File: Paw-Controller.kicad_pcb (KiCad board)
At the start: 2 copper layers, 41 x 24 mm, 26 parts, among them J1 Conn_02x06_Odd_Even, J2 Conn_01x08, J3 Conn_01x02, Q1 DMN1019USN, Q2 DMN1019USN, Q3 DMN1019USN, SW1 SW_SPST_KMR2, U1 LMZ10503, U2 ATSAMD21E18A-AF

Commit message: Added missing PWM labels.
Signed-off-by: Aaron Williams <aaron.w2@gmail.com>
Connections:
- net Net-(D1-Pad2) renamed /PWM0
- net Net-(D2-Pad2) renamed /PWM1
- net Net-(D3-Pad2) renamed /PWM2

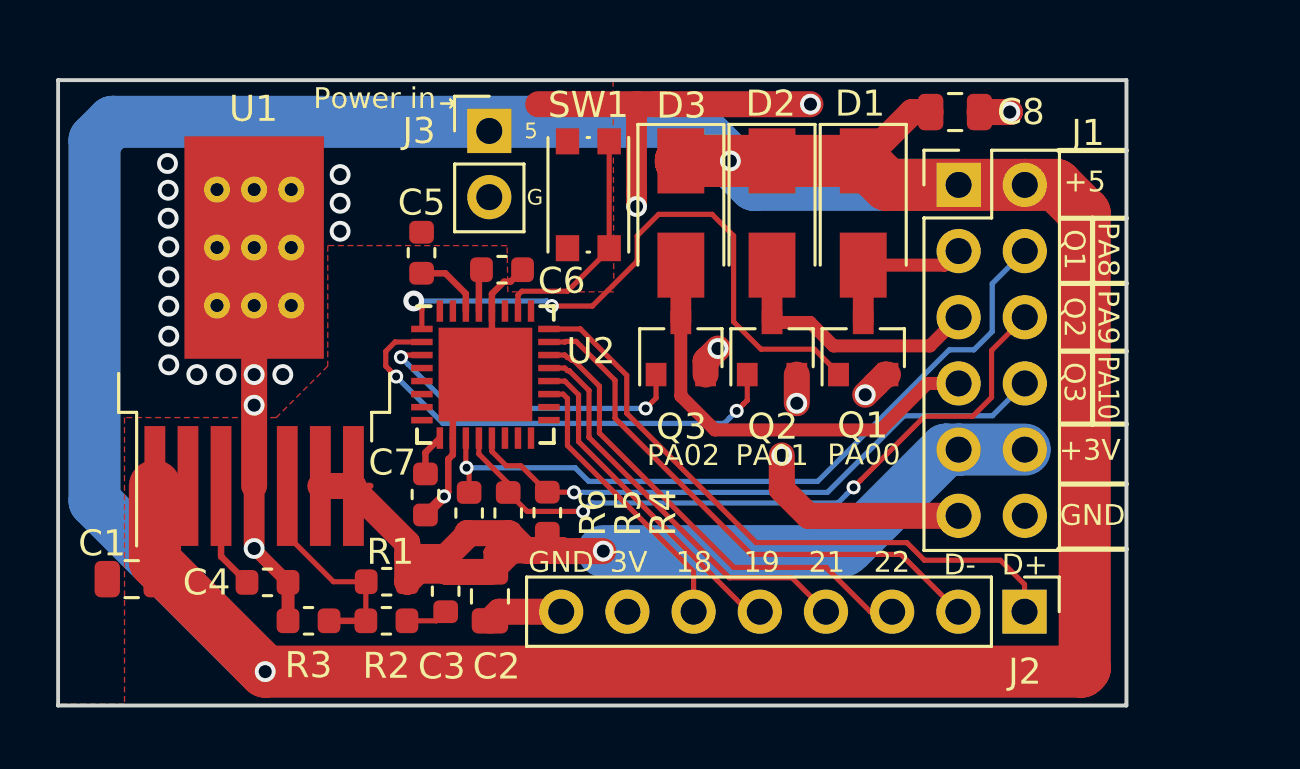
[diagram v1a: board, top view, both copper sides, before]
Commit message: Version 2.0 converts each PWM channel to use an H-bridge.
This allows the controller to be able to drive a 3V brushless motor.  The
M0 processor is capable of generating the timing for the motors, though at
this time I don't know if it works with 6 GPIO pins or only with three.

Six was chosen so that a PWMs can be set to a high impedence state.  This
is useful in the case where multiple brushed motors are attached between either
+3v or ground and the PWM pin, though the alternative is to just pull the PWM
output to the same level.  That might be version 2.1 later.

Signed-off-by: Aaron Williams <aaron.w2@gmail.com>
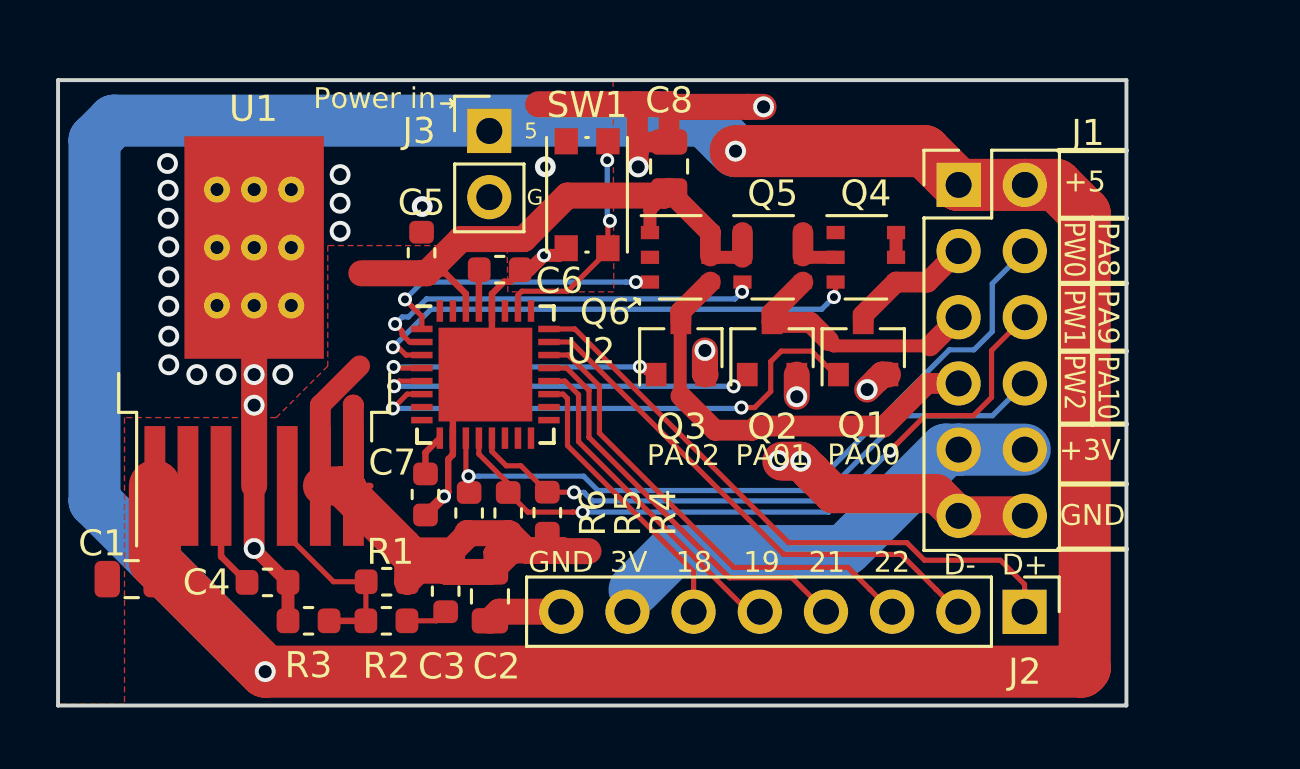
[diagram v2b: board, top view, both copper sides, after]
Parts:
- removed D1, D2, D3: B120-E3, Diode_SMD:D_SMA
- added Q4: SI3493DDV-T1-GE3, Package_SO:TSOP-6_1.65x3.05mm_P0.95mm, F.Cu at (80.0, 69.8)
- added Q5: SI3493DDV-T1-GE3, Package_SO:TSOP-6_1.65x3.05mm_P0.95mm, F.Cu at (76.4, 69.8)
- added Q6: SI3493DDV-T1-GE3, Package_SO:TSOP-6_1.65x3.05mm_P0.95mm, F.Cu at (72.9, 69.8)
- moved C8 11.2 mm to (72.5, 66.3), turned to 90 degrees
- moved C6 0.09 mm to (66.0, 70.3)
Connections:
- C8 pad 1: +5V -> +3V3
- Q1 pad 1: /PA00 -> /PA05
- Q2 pad 1: /PA01 -> /PA04
- Q3 pad 1: /PA02 -> /PA03
- U2 pad 4: Net-(U2-Pad4) -> /PA03
- U2 pad 5: Net-(U2-Pad5) -> /PA04
- U2 pad 6: Net-(U2-Pad6) -> /PA05
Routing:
- net +3V3: track 47.9 -> 85.4 mm, vias 1 -> 0
- net /PA05: track 0.00 -> 20.4 mm, vias 0 -> 2
- net +5V: track 138.3 -> 122.0 mm
- net /PA04: track 0.00 -> 14.9 mm, vias 0 -> 2
- net /PA00: track 24.1 -> 11.1 mm
- net /PA03: track 0.00 -> 11.3 mm, vias 0 -> 2
- net /PA02: track 12.5 -> 19.6 mm
- net /PA01: track 18.2 -> 15.6 mm
- net GND: track 58.1 -> 59.4 mm, vias 25 -> 28
- net /D_N: track 20.9 -> 20.0 mm
- net /D_P: track 24.2 -> 23.4 mm
- net /PWM2: track 17.0 -> 17.7 mm
- net Net-(SW1-Pad2): track 8.99 -> 9.07 mm, vias 0 -> 2
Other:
- board text added: "Do not exceed 5V for PWM0, PWM1 or PWM2."
- board text added: "PW0"
- board text added: "PW1"
- board text added: "PW2"
- board text added: "Rev 2.0"
- board text removed: "Do not exceed 5V for Q0, Q1 and Q2 due to protection diodes."
- board text removed: "Q1"
- board text removed: "Q2"
- board text removed: "Q3"
- board text removed: "Rev 1.0"

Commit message: Fixed solder mask clearance.
Signed-off-by: Aaron Williams <aaron.w2@gmail.com>
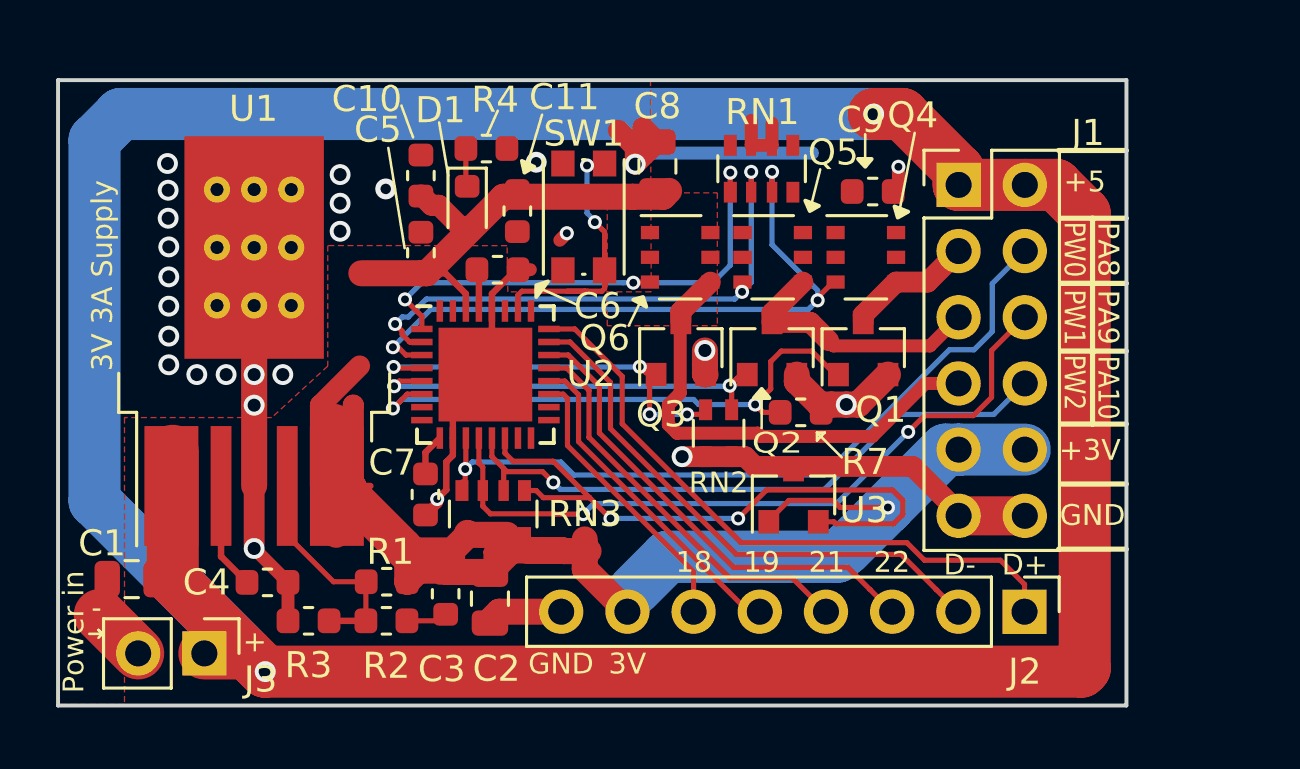
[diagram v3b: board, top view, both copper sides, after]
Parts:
- removed R5, R6: 10K, Resistor_SMD:R_0603_1608Metric
- added C10: 1uF, Capacitor_SMD:C_0603_1608Metric, F.Cu at (62.9, 66.7)
- added C11: 0.1uF, Capacitor_SMD:C_0603_1608Metric, F.Cu at (66.6, 68.0)
- added C9: 0.1uF, Capacitor_SMD:C_0603_1608Metric, F.Cu at (80.3, 67.3)
- added D1: LED, LED_SMD:LED_0603_1608Metric, F.Cu at (64.7, 67.9)
- added R7: 100K, Resistor_SMD:R_0603_1608Metric, F.Cu at (77.5, 75.8)
- added RN1: 100K, Resistor_SMD:R_Array_Convex_4x0603, F.Cu at (76.0, 66.4)
- added RN2: 100K, Resistor_SMD:R_Array_Convex_2x0603, F.Cu at (74.3, 76.5)
- added RN3: 10K, Resistor_SMD:R_Array_Convex_4x0603, F.Cu at (65.7, 79.7)
- added U3: DRV5032FCDBZT, Package_TO_SOT_SMD:SOT-23, F.Cu at (77.2, 79.0)
- R4: value 10K -> 330
- moved J3 22.8 mm to (54.6, 85.0), turned to 270 degrees
- moved R4 14.2 mm to (65.4, 65.6), turned to 180 degrees
- moved SW1 0.86 mm to (69.2, 68.2)
- moved C8 0.45 mm to (72.0, 66.3)
- moved C3 0.10 mm to (63.9, 82.7)
- moved C2 0.09 mm to (65.6, 82.9)
- moved C6 0.09 mm to (65.9, 70.3)
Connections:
- R4 pad 1: +3V3 -> GND
- R4 pad 2: /PA10 -> Net-(D1-Pad1)
- U2 pad 14: Net-(U2-Pad14) -> /PA11
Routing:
- net /PA11: track 0.00 -> 24.1 mm, vias 0 -> 2
- net /PA00: track 11.1 -> 19.4 mm, vias 2 -> 3
- net GND: track 59.4 -> 66.1 mm, vias 28 -> 26
- net /PA02: track 19.6 -> 25.8 mm, vias 2 -> 3
- net /PA01: track 15.6 -> 21.1 mm, vias 2 -> 3
- net +3V3: track 85.4 -> 90.6 mm, vias 0 -> 1
- net +5V: track 122.0 -> 126.2 mm
- net /PA03: track 11.3 -> 15.2 mm, vias 2 -> 4
- net Net-(D1-Pad1): track 0.00 -> 1.52 mm
- net Net-(SW1-Pad2): track 9.07 -> 10.4 mm
- net /PA05: track 20.4 -> 21.6 mm
- net /D_P: track 23.4 -> 24.4 mm
- net /D_N: track 20.0 -> 21.0 mm
- net /PA04: track 14.9 -> 15.8 mm
- net /PA09: track 26.8 -> 27.8 mm
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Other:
- rule pad_to_mask_clearance: 0.0508 -> -0.0508
- board text added: "+"
- board text added: "-"
- board text added: "3V 3A Supply"
- board text added: "Do not exceed 3V for PWM0, PWM1 or PWM2."
- board text added: "Rev 2.1.1"
- board text removed: "5"
- board text removed: "Do not exceed 5V for PWM0, PWM1 or PWM2."
- board text removed: "G"
- board text removed: "PA00"
- board text removed: "PA01"
- board text removed: "PA02"
- board text removed: "Rev 2.0"

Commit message: Fixed P-CH mosfets and changed to more readily available mosfet.
Signed-off-by: Aaron Williams <aaron.w2@gmail.com>
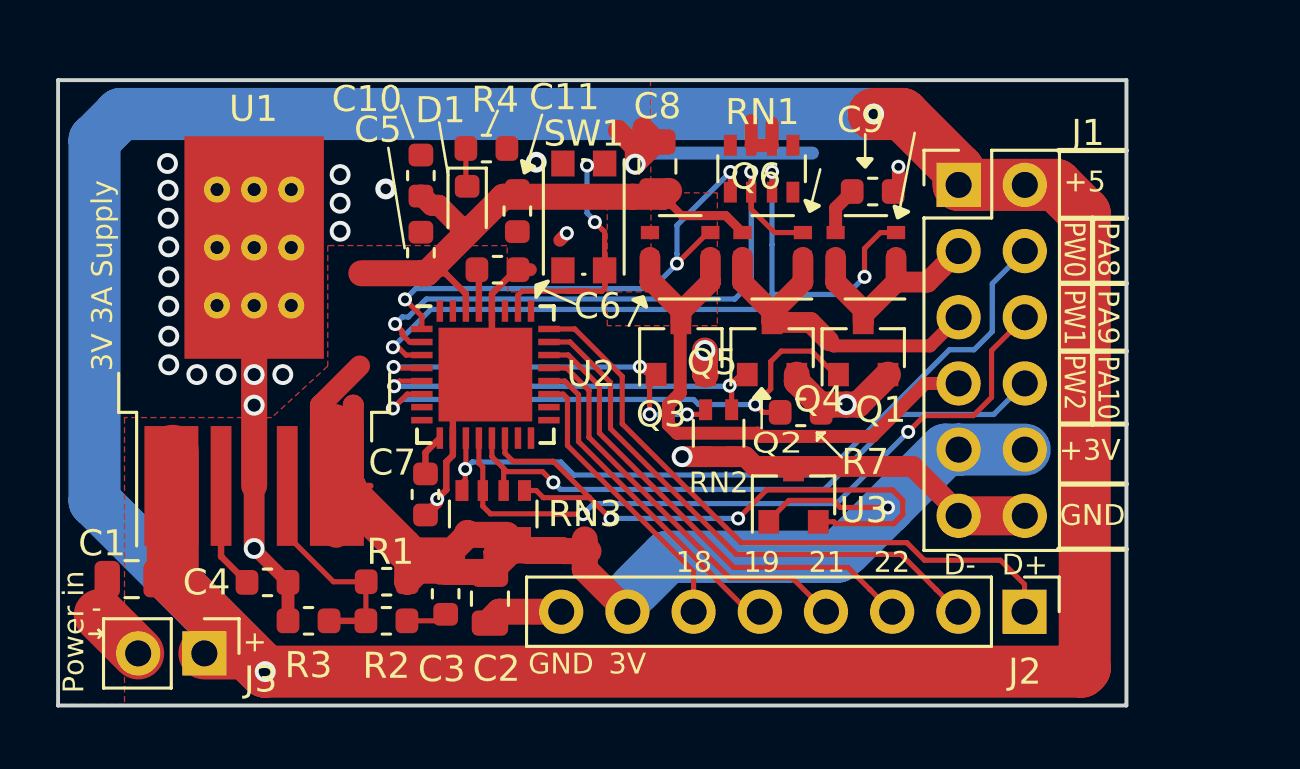
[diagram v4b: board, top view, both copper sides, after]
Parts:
- turned Q4 to 180 degrees
- turned Q5 to 180 degrees
- turned Q6 to 180 degrees
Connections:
- Q4 pad 1: +3V3 -> /PWM0
- Q4 pad 2: +3V3 -> /PWM0
- Q4 pad 4: /PWM0 -> +3V3
- Q4 pad 5: +3V3 -> /PWM0
- Q4 pad 6: +3V3 -> /PWM0
- Q5 pad 1: +3V3 -> /PWM1
- Q5 pad 2: +3V3 -> /PWM1
- Q5 pad 4: /PWM1 -> +3V3
- Q5 pad 5: +3V3 -> /PWM1
- Q5 pad 6: +3V3 -> /PWM1
- Q6 pad 1: +3V3 -> /PWM2
- Q6 pad 2: +3V3 -> /PWM2
- Q6 pad 4: /PWM2 -> +3V3
- Q6 pad 5: +3V3 -> /PWM2
- Q6 pad 6: +3V3 -> /PWM2
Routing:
- net +3V3: track 90.6 -> 96.8 mm
- net /PWM0: track 5.73 -> 9.71 mm
- net /PWM1: track 10.0 -> 14.0 mm
- net /PWM2: track 18.5 -> 22.1 mm
- net /PA02: track 25.8 -> 28.5 mm
- net /PA01: track 21.1 -> 23.8 mm, vias 3 -> 2
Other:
- board text added: "Rev 2.1.2"
- board text removed: "Rev 2.1.1"

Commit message: Add another push/pull channel
This adds a 4th push/pull channel and exports PA17 to J1.

Due to the increase in board size, two more pins were added to J2,
an additional +5 and ground pin for USB.

Updated to version 2.2.0

Signed-off-by: Aaron Williams <aaron.w2@gmail.com>
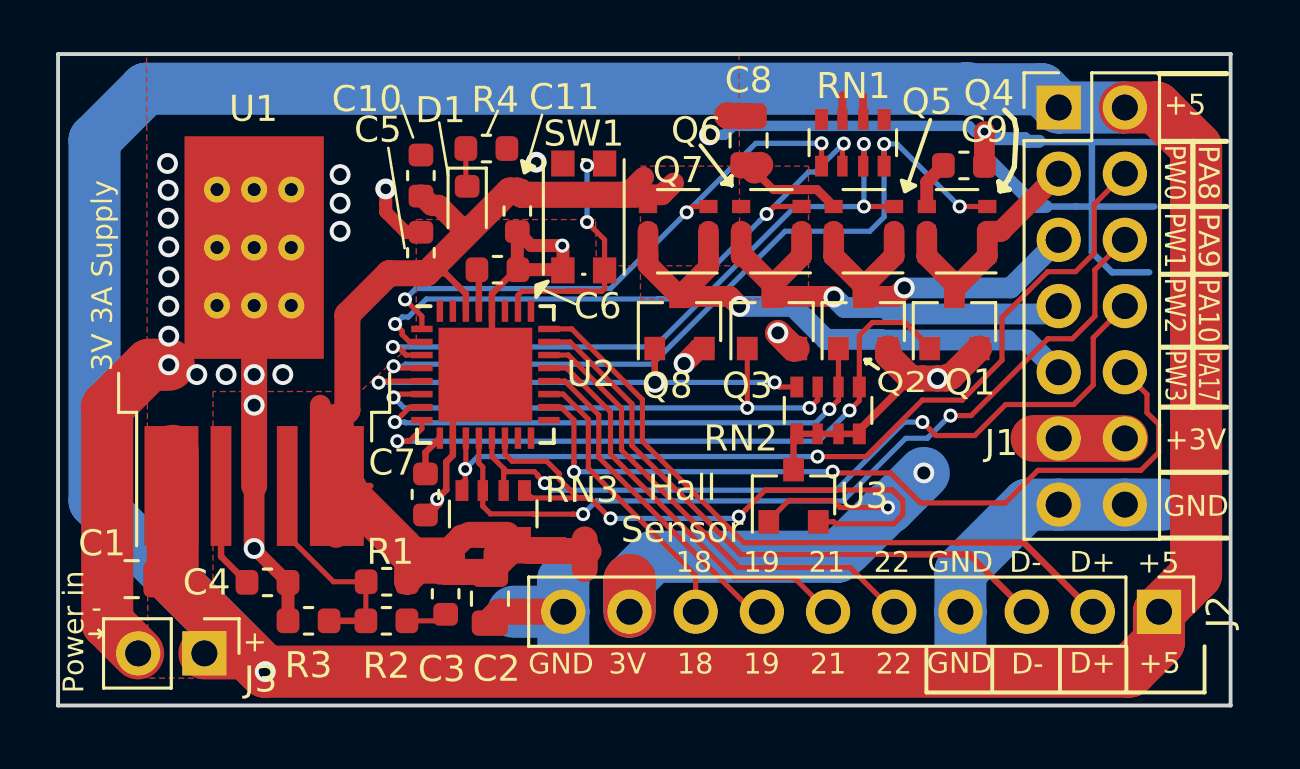
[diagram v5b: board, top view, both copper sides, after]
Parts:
- removed R7: 100K, Resistor_SMD:R_0603_1608Metric
- added Q7: SI3407DV-T1-GE3, Package_SO:TSOP-6_1.65x3.05mm_P0.95mm, F.Cu at (72.8, 68.8)
- added Q8: DMN1019USN, Package_TO_SOT_SMD:SOT-23, F.Cu at (72.8, 72.3)
- J1: value Conn_02x06_Odd_Even -> Conn_02x07_Odd_Even; footprint Connector_PinHeader_2.54mm:PinHeader_2x06_P2.54mm_Vertical -> Connector_PinHeader_2.54mm:PinHeader_2x07_P2.54mm_Vertical
- J2: value Conn_01x08 -> Conn_01x10; footprint Connector_PinHeader_2.54mm:PinHeader_1x08_P2.54mm_Vertical -> Connector_PinHeader_2.54mm:PinHeader_1x10_P2.54mm_Vertical
- Q4, Q5, Q6: value SI3493DDV-T1-GE3 -> SI3407DV-T1-GE3
- RN2: footprint Resistor_SMD:R_Array_Convex_2x0603 -> Resistor_SMD:R_Array_Convex_4x0603
- moved J2 5.16 mm to (91.2, 83.4)
- moved J1 4.85 mm to (87.4, 64.0)
- moved RN2 4.29 mm to (78.5, 75.7)
- moved C8 3.64 mm to (75.5, 65.3)
- moved C9 3.64 mm to (83.8, 66.3)
- moved Q1 3.64 mm to (83.4, 72.3)
- moved Q2 3.64 mm to (79.9, 72.3)
- moved Q3 3.64 mm to (76.4, 72.3)
- moved Q4 3.64 mm to (83.5, 68.8)
- moved Q5 3.64 mm to (79.9, 68.8)
- moved Q6 3.64 mm to (76.4, 68.8)
- moved RN1 3.64 mm to (79.5, 65.4)
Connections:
- J1 pad 10: +3V3 -> /PA17
- J1 pad 11: GND -> +3V3
- J1 pad 12: GND -> +3V3
- J1 pad 9: +3V3 -> /PWM3
- J2 pad 1: /D_P -> +5V
- J2 pad 2: /D_N -> /D_P
- J2 pad 3: /PA22 -> /D_N
- J2 pad 4: /PA21 -> GND
- J2 pad 5: /PA19 -> /PA22
- J2 pad 6: /PA18 -> /PA21
- J2 pad 7: +3V3 -> /PA19
- J2 pad 8: GND -> /PA18
- Q1 pad 1: /PA05 -> /PA07
- Q2 pad 1: /PA04 -> /PA06
- Q3 pad 1: /PA03 -> /PA05
- Q4 pad 3: /PA02 -> /PA03
- Q5 pad 3: /PA01 -> /PA02
- Q6 pad 3: /PA00 -> /PA01
- RN1 pad 4: Net-(RN1-Pad4) -> /PA03
- RN1 pad 5: Net-(RN1-Pad5) -> +3V3
- RN2 pad 3: /PA04 -> GND
- RN2 pad 4: /PA03 -> GND
- U2 pad 18: Net-(U2-Pad18) -> /PA17
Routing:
- net GND: track 66.1 -> 117.9 mm
- net /PA17: track 0.00 -> 30.5 mm, vias 0 -> 2
- net /PA07: track 0.00 -> 25.7 mm, vias 0 -> 2
- net /PWM3: track 0.00 -> 21.7 mm, vias 0 -> 1
- net /PA06: track 0.00 -> 20.7 mm, vias 0 -> 2
- net /PA03: track 15.2 -> 31.1 mm, vias 4 -> 3
- net +5V: track 126.2 -> 135.4 mm, vias 2 -> 1
- net /PA10: track 24.2 -> 30.8 mm, vias 1 -> 2
- net /PA08: track 28.7 -> 34.3 mm, vias 1 -> 2
- net /PA09: track 27.8 -> 32.8 mm
- net /PWM2: track 22.1 -> 17.0 mm, vias 0 -> 1
- net /PA04: track 15.8 -> 19.1 mm, vias 2 -> 3
- net /PA02: track 28.5 -> 26.0 mm
- net /D_N: track 21.0 -> 23.6 mm
- net /PA00: track 19.3 -> 21.7 mm
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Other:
- board size 41 x 24 mm -> 45 x 25 mm
- board text added: "Copyright © 2019 by Aaron Williams"
- board text added: "Hall Sensor"
- board text added: "PA17"
- board text added: "PW3"
- board text added: "Rev 2.2.0"
- board text removed: "Copyright © 2018 by Aaron Williams"
- board text removed: "Rev 2.1.2"

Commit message: Fixed silkscreen and solder mask.
Signed-off-by: Aaron Williams <aaron.w2@gmail.com>
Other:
- rule pad_to_mask_clearance: -0.0508 -> 0.0508
- board text added: "Do not exceed 3V for PWM0, PWM1, PWM2 or PWM3."
- board text added: "Rev 2.2.1"
- board text removed: "Do not exceed 3V for PWM0, PWM1 or PWM2."
- board text removed: "Rev 2.2.0"
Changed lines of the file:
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@@
   (title_block
     (title "Paw Controller")
-    (date 2019-01-29)
-    (rev 2.2.0)
-    (company "Copyright © 2018 by Aaron Williams")
+    (date 2019-02-04)
+    (rev 2.2.1)
+    (company "Copyright © 2018-2019 by Aaron Williams")
   )
   (layers
@@
     (pad_size 1.7 1.7)
     (pad_drill 1)
-    (pad_to_mask_clearance -0.0508)
+    (pad_to_mask_clearance 0.0508)
     (solder_mask_min_width 0.25)
     (aux_axis_origin 0 0)
@@
     (effects (font (size 0.8 0.8) (thickness 0.1)))
   )
-  (gr_text "Rev 2.2.0" (at 60.025 82.65) (layer B.SilkS)
+  (gr_text "Rev 2.2.1" (at 60.025 82.65) (layer B.SilkS)
     (effects (font (size 1.5 1.5) (thickness 0.3)) (justify mirror))
   )
-  (gr_text "Do not exceed 3V for\nPWM0, PWM1 or PWM2." (at 69.85 72.775) (layer B.SilkS)
+  (gr_text "Do not exceed 3V for\nPWM0, PWM1, PWM2 or PWM3." (at 71.1 71.7) (layer B.SilkS)
     (effects (font (size 1.2 1.2) (thickness 0.2)) (justify mirror))
   )
